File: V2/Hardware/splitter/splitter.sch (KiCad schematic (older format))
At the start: 17 parts, among them J0 Rpi_40Pin_F, J1 Control1_F, J2 Control2_F, J3 Control3_F, J4 Molex_PSU_F, J5 Siren, J6 USB_A_F, K0 RELRAS0515, Q0 BC548C, Q1 BD139-16

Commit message: update schemas
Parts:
- added D3: LED_2V_20mA, LED_THT:LED_D5.0mm, symbol Device:LED
- added R4: 510R, Resistor_THT:R_Axial_DIN0207_L6.3mm_D2.5mm_P10.16mm_Horizontal, symbol Device:R
- J1: value Control1_F -> Control_seg:1
- J2: value Control2_F -> Control_seg:2
- J3: value Control3_F -> Control_seg:3
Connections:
- net 12V+: now also R4.2
- net Earth: now also D3.1 (K)
- net seg:2_bit:a_gpio:10: now reaches J0.19 (Pin_19)
- net seg:2_bit:a_gpio:10: now also J2.4 (Pin_4)
- net seg:2_bit:b_gpio:09: now reaches J0.21 (Pin_21)
- net seg:2_bit:b_gpio:09: now also J2.3 (Pin_3)
- net seg:2_bit:c_gpio:11: now reaches J0.23 (Pin_23)
- net seg:2_bit:c_gpio:11: now also J2.2 (Pin_2)
- net seg:3_bit:d_gpio:26: now reaches J0.37 (Pin_37)
- net seg:3_bit:d_gpio:26: now also J3.1 (Pin_1)
- net 1a renamed seg:1_bit:d_gpio:22
- net 1b renamed seg:1_bit:c_gpio:27
- net 1c renamed seg:1_bit:b_gpio:17
- net 1d renamed seg:1_bit:a_gpio:04
- net 2a renamed seg:2_bit:d_gpio:05
- net seg:2_bit:d_gpio:05: now also J0.29 (Pin_29); no longer J0.35 (Pin_35)
- net 2b renamed seg:3_bit:b_gpio:13
- net seg:3_bit:b_gpio:13: now also J3.3 (Pin_3); no longer J2.2 (Pin_2)
- net 2c renamed seg:3_bit:a_gpio:06
- net seg:3_bit:a_gpio:06: now also J3.4 (Pin_4); no longer J2.3 (Pin_3)
- removed net 2d: J0.29 (Pin_29), J2.4 (Pin_4)
- net 3a renamed SIREN_gpio:21
- net SIREN_gpio:21: now also R1.2; no longer J3.1 (Pin_1)
- net 3b: no longer names the net of J0.38 (Pin_38)
- net 3b: no longer J3.2 (Pin_2)
- net 3c: no longer names the net of J0.36 (Pin_36)
- net 3c: no longer J3.3 (Pin_3)
- net 3d: no longer names the net of J0.32 (Pin_32)
- net 3d: no longer J3.4 (Pin_4)
- removed net BLANKING: J0.12 (Pin_12), J1.5 (Pin_5), J2.5 (Pin_5), J3.5 (Pin_5)
- net SIREN: no longer names the net of J0.16 (Pin_16)
- net SIREN: no longer R1.2
- new net: D3.2 (A), R4.1
- new net seg:3_bit:c_gpio:19: J0.35 (Pin_35), J3.2 (Pin_2)
- no-connect marks 32 -> 36
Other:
- moved on the sheet: D0, D1, D2, J0, J1, J2, J3, J4, J5, J6, K0, Q0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

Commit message: Finish PCBs
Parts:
- Q0: footprint Package_TO_SOT_THT:TO-92_Inline -> Package_TO_SOT_THT:TO-92_Inline_Wide
- R0: value 150R -> 33k
- R3, R4: value 510R -> 33k
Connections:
- net seg:1_bit:a_gpio:04: now also J1.6 (Pin_6); no longer J1.4 (Pin_4)
- net seg:1_bit:b_gpio:17: now also J1.5 (Pin_5); no longer J1.3 (Pin_3)
- net seg:1_bit:c_gpio:27: now also J1.3 (Pin_3); no longer J1.2 (Pin_2)
- net seg:2_bit:a_gpio:10: now also J2.6 (Pin_6); no longer J2.4 (Pin_4)
- net seg:2_bit:b_gpio:09: now also J2.5 (Pin_5); no longer J2.3 (Pin_3)
- net seg:2_bit:c_gpio:11: now also J2.3 (Pin_3); no longer J2.2 (Pin_2)
- net seg:3_bit:a_gpio:06: now also J3.6 (Pin_6); no longer J3.4 (Pin_4)
- net seg:3_bit:b_gpio:13: now also J3.5 (Pin_5); no longer J3.3 (Pin_3)
- net seg:3_bit:c_gpio:19: now also J3.3 (Pin_3); no longer J3.2 (Pin_2)
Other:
- moved on the sheet: J2, J3
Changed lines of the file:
@@
 L Connector_Generic:Conn_02x03_Counter_Clockwise J2
 U 1 1 5EA23348
-P 3950 4300
-F 0 "J2" H 4000 4617 50  0000 C CNN
-F 1 "Control_seg:2" H 4000 4526 50  0000 C CNN
-F 2 "Connector_PinHeader_2.54mm:PinHeader_2x03_P2.54mm_Horizontal" H 3950 4300 50  0001 C CNN
-F 3 "~" H 3950 4300 50  0001 C CNN
-	1    3950 4300
-	0    -1   -1   0
-$EndComp
-$Comp
-L Connector_Generic:Conn_02x03_Counter_Clockwise J3
-U 1 1 5EA246A5
-P 3450 5050
-F 0 "J3" H 3500 5367 50  0000 C CNN
-F 1 "Control_seg:3" H 3500 5276 50  0000 C CNN
-F 2 "Connector_PinHeader_2.54mm:PinHeader_2x03_P2.54mm_Horizontal" H 3450 5050 50  0001 C CNN
-F 3 "~" H 3450 5050 50  0001 C CNN
-	1    3450 5050
+P 3850 4300
+F 0 "J2" H 3900 4617 50  0000 C CNN
+F 1 "Control_seg:2" H 3900 4526 50  0000 C CNN
+F 2 "Connector_PinHeader_2.54mm:PinHeader_2x03_P2.54mm_Horizontal" H 3850 4300 50  0001 C CNN
+F 3 "~" H 3850 4300 50  0001 C CNN
+	1    3850 4300
 	0    -1   -1   0
 $EndComp
@@
 P 4450 2100
 F 0 "R0" H 4520 2146 50  0000 L CNN
-F 1 "150R" H 4520 2055 50  0000 L CNN
+F 1 "33k" H 4520 2055 50  0000 L CNN
 F 2 "Resistor_THT:R_Axial_DIN0207_L6.3mm_D2.5mm_P10.16mm_Horizontal" V 4380 2100 50  0001 C CNN
 F 3 "~" H 4450 2100 50  0001 C CNN
@@
 F 0 "Q0" H 7041 4446 50  0000 L CNN
 F 1 "BC548C" H 7041 4355 50  0000 L CNN
-F 2 "Package_TO_SOT_THT:TO-92_Inline" H 7050 4325 50  0001 L CIN
+F 2 "Package_TO_SOT_THT:TO-92_Inline_Wide" H 7050 4325 50  0001 L CIN
 F 3 "http://www.fairchildsemi.com/ds/BC/BC547.pdf" H 6850 4400 50  0001 L CNN
 	1    6850 4400
@@
 P 7250 3400
 F 0 "R3" H 7320 3446 50  0000 L CNN
-F 1 "510R" H 7320 3355 50  0000 L CNN
+F 1 "33k" H 7320 3355 50  0000 L CNN
 F 2 "Resistor_THT:R_Axial_DIN0207_L6.3mm_D2.5mm_P10.16mm_Horizontal" V 7180 3400 50  0001 C CNN
 F 3 "~" H 7250 3400 50  0001 C CNN
@@
 seg:3_bit:d_gpio:26
 Wire Wire Line
-	5600 4000 4700 4000
-Wire Wire Line
-	3850 5100 5600 5100
-Wire Wire Line
-	4700 4000 4700 3450
-Wire Wire Line
-	4700 3450 4550 3450
-Wire Wire Line
-	4350 4400 4350 3950
-Wire Wire Line
-	4350 4400 5600 4400
-Wire Wire Line
-	4450 4300 4450 3950
-Wire Wire Line
-	4450 4300 5600 4300
-Wire Wire Line
-	4550 4200 4550 3950
-Wire Wire Line
-	4550 4200 5600 4200
-Wire Wire Line
-	4200 4600 4200 4000
-Wire Wire Line
-	4200 4000 4050 4000
-Wire Wire Line
-	4200 4600 5600 4600
-Wire Wire Line
-	3850 5100 3850 4500
-Wire Wire Line
-	3950 4800 3950 4500
-Wire Wire Line
-	3950 4800 5600 4800
-Wire Wire Line
-	4050 4700 4050 4500
+	4750 4200 5600 4200
 Wire Wire Line
 	4050 4700 5600 4700
 Wire Wire Line
-	3700 5200 3700 4750
-Wire Wire Line
-	3700 4750 3550 4750
-Wire Wire Line
-	3700 5200 5600 5200
-Wire Wire Line
-	3550 5300 3550 5250
-Wire Wire Line
-	3550 5300 5600 5300
-Wire Wire Line
-	3450 5400 3450 5250
-Wire Wire Line
-	3450 5400 5600 5400
-Wire Wire Line
-	3350 5500 3350 5250
-Wire Wire Line
-	3350 5500 5600 5500
-NoConn ~ 4350 3450
-NoConn ~ 4450 3450
-NoConn ~ 3850 4000
-NoConn ~ 3950 4000
-NoConn ~ 3350 4750
-NoConn ~ 3450 4750
+	3450 5300 5600 5300
 $Comp
 L Device:R R4
@@
 P 5450 2550
 F 0 "R4" H 5520 2596 50  0000 L CNN
-F 1 "510R" H 5520 2505 50  0000 L CNN
+F 1 "33k" H 5520 2505 50  0000 L CNN
 F 2 "Resistor_THT:R_Axial_DIN0207_L6.3mm_D2.5mm_P10.16mm_Horizontal" V 5380 2550 50  0001 C CNN
 F 3 "~" H 5450 2550 50  0001 C CNN
@@
 Wire Wire Line
 	6300 2400 6600 2400
+Wire Wire Line
+	4850 4000 5600 4000
+Wire Wire Line
+	4750 4200 4750 3400
+Wire Wire Line
+	4750 3400 4450 3400
+Wire Wire Line
+	4450 3400 4450 3450
+Wire Wire Line
+	4550 4300 5600 4300
+Wire Wire Line
+	4150 4600 5600 4600
+Wire Wire Line
+	4050 4700 4050 3950
+Wire Wire Line
+	4050 3950 3850 3950
+Wire Wire Line
+	3850 3950 3850 4000
+Wire Wire Line
+	3950 4800 5600 4800
+Wire Wire Line
+	3550 5200 5600 5200
+Wire Wire Line
+	3450 5300 3450 4500
+Wire Wire Line
+	3450 4500 3250 4500
+Wire Wire Line
+	3350 5400 5600 5400
+NoConn ~ 3950 4000
+NoConn ~ 4550 3450
+Wire Wire Line
+	4550 4300 4550 3950
+Wire Wire Line
+	4350 4400 4350 3950
+Wire Wire Line
+	4350 4400 5600 4400
+Wire Wire Line
+	4850 4000 4850 3350
+Wire Wire Line
+	4850 3350 4350 3350
+Wire Wire Line
+	4350 3350 4350 3450
+NoConn ~ 4450 3950
+Wire Wire Line
+	3950 4800 3950 4500
+Wire Wire Line
+	4150 4600 4150 3900
+Wire Wire Line
+	4150 3900 3750 3900
+Wire Wire Line
+	3750 3900 3750 4000
+Wire Wire Line
+	3750 5100 5600 5100
+Wire Wire Line
+	3750 5100 3750 4500
+Wire Wire Line
+	3250 4500 3250 4550
+NoConn ~ 3350 4550
+$Comp
+L Connector_Generic:Conn_02x03_Counter_Clockwise J3
+U 1 1 5EA246A5
+P 3250 4850
+F 0 "J3" H 3300 5167 50  0000 C CNN
+F 1 "Control_seg:3" H 3300 5076 50  0000 C CNN
+F 2 "Connector_PinHeader_2.54mm:PinHeader_2x03_P2.54mm_Horizontal" H 3250 4850 50  0001 C CNN
+F 3 "~" H 3250 4850 50  0001 C CNN
+	1    3250 4850
+	0    -1   -1   0
+$EndComp
+Wire Wire Line
+	3350 5400 3350 5050
+Wire Wire Line
+	3150 5500 3150 5050
+Wire Wire Line
+	3150 5500 5600 5500
+Wire Wire Line
+	3550 5200 3550 4450
+Wire Wire Line
+	3550 4450 3150 4450
+Wire Wire Line
+	3150 4450 3150 4550
+NoConn ~ 3850 4500
+NoConn ~ 3250 5050
 $EndSCHEMATC

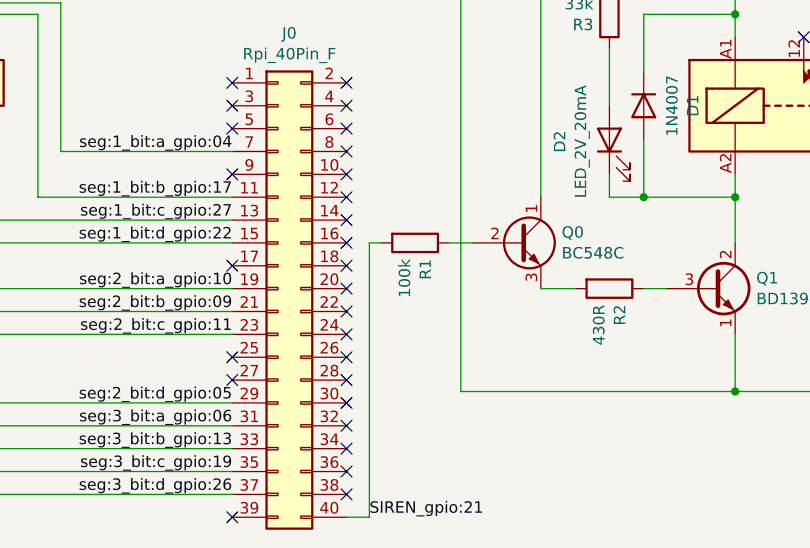
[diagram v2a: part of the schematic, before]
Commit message: Fix relay symbol
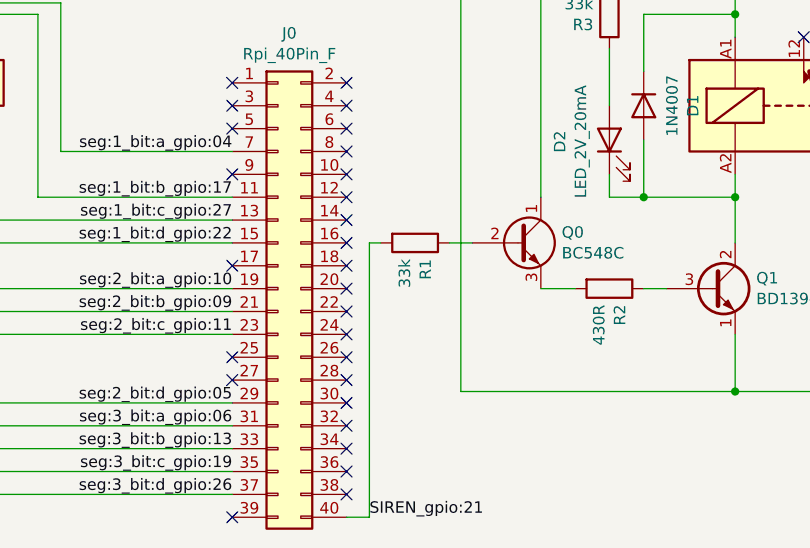
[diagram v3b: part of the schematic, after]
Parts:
- K0: footprint Relay_THT:Relay_SPDT_Finder_40.31 -> Relay_THT:Relay_SPDT_Finder_36.11
- R1: value 100k -> 33k
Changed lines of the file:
@@
 F 0 "K0" H 8430 3846 50  0000 L CNN
 F 1 "RELRAS0515" H 8430 3755 50  0000 L CNN
-F 2 "Relay_THT:Relay_SPDT_Finder_40.31" H 9140 3760 50  0001 C CNN
+F 2 "Relay_THT:Relay_SPDT_Finder_36.11" H 9140 3760 50  0001 C CNN
 F 3 "http://gfinder.findernet.com/assets/Series/353/S40EN.pdf" H 8000 3800 50  0001 C CNN
 	1    8000 3800
@@
 P 6400 4400
 F 0 "R1" H 6470 4446 50  0000 L CNN
-F 1 "100k" H 6470 4355 50  0000 L CNN
+F 1 "33k" H 6470 4355 50  0000 L CNN
 F 2 "Resistor_THT:R_Axial_DIN0207_L6.3mm_D2.5mm_P10.16mm_Horizontal" V 6330 4400 50  0001 C CNN
 F 3 "~" H 6400 4400 50  0001 C CNN

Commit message: Update splitter board
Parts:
- J0: footprint Connector_PinHeader_2.54mm:PinHeader_2x20_P2.54mm_Vertical -> Connector_IDC:IDC-Header_2x20_P2.54mm_Vertical
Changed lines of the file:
@@
 F 0 "J0" H 5850 5717 50  0000 C CNN
 F 1 "Rpi_40Pin_F" H 5850 5626 50  0000 C CNN
-F 2 "Connector_PinHeader_2.54mm:PinHeader_2x20_P2.54mm_Vertical" H 5800 4600 50  0001 C CNN
+F 2 "Connector_IDC:IDC-Header_2x20_P2.54mm_Vertical" H 5800 4600 50  0001 C CNN
 F 3 "~" H 5800 4600 50  0001 C CNN
 	1    5800 4600

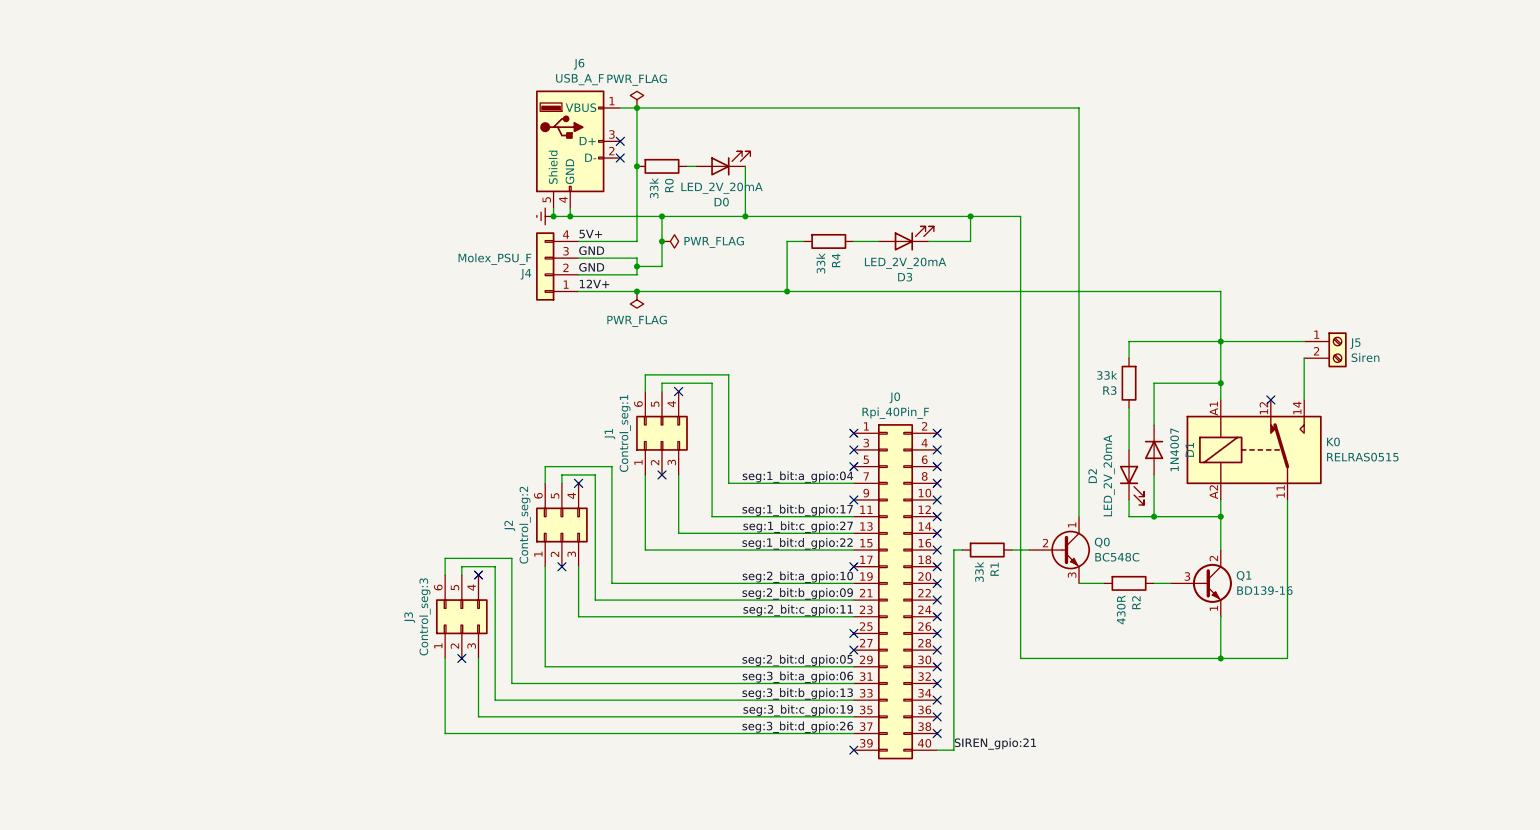
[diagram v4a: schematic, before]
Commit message: Simplify relay control
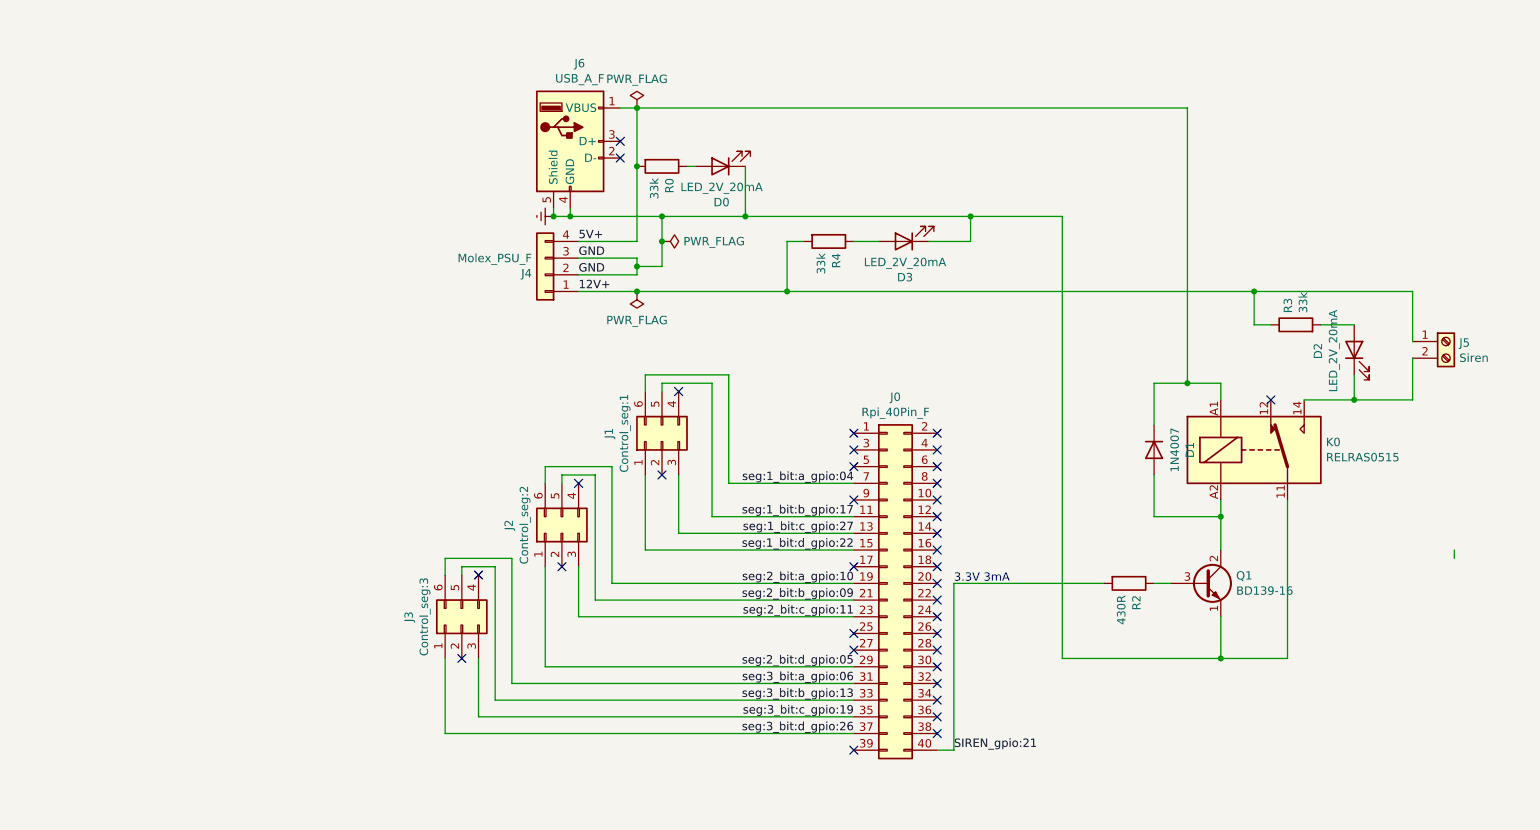
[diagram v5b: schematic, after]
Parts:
- removed Q0: BC548C, Package_TO_SOT_THT:TO-92_Inline_Wide, symbol Transistor_BJT:BC548
- removed R1: 33k, Resistor_THT:R_Axial_DIN0207_L6.3mm_D2.5mm_P10.16mm_Horizontal, symbol Device:R
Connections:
- net 12V+: now also R3.1; no longer D1.1 (K), K0.A1, R3.2
- net 5V+: now also D1.1 (K), K0.A1
- net SIREN_gpio:21: now also R2.2
- net at J5.2 (Pin_2), K0.14: now also D2.1 (K)
- net at D1.2 (A), K0.A2, Q1.2 (C): no longer D2.1 (K)
- net at D2.2 (A): now also R3.2; no longer R3.1
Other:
- note added: "3.3V 3mA"
- moved on the sheet: D2, J5, R3
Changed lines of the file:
@@
 L Connector:Screw_Terminal_01x02 J5
 U 1 1 5EBB14C8
-P 8500 3150
-F 0 "J5" H 8580 3142 50  0000 L CNN
-F 1 "Siren" H 8580 3051 50  0000 L CNN
-F 2 "TerminalBlock:TerminalBlock_bornier-2_P5.08mm" H 8500 3150 50  0001 C CNN
-F 3 "~" H 8500 3150 50  0001 C CNN
-	1    8500 3150
+P 9150 3150
+F 0 "J5" H 9230 3142 50  0000 L CNN
+F 1 "Siren" H 9230 3051 50  0000 L CNN
+F 2 "TerminalBlock:TerminalBlock_bornier-2_P5.08mm" H 9150 3150 50  0001 C CNN
+F 3 "~" H 9150 3150 50  0001 C CNN
+	1    9150 3150
 	1    0    0    -1
 $EndComp
@@
 $EndComp
 $Comp
-L Transistor_BJT:BC548 Q0
-U 1 1 5ED48271
-P 6850 4400
-F 0 "Q0" H 7041 4446 50  0000 L CNN
-F 1 "BC548C" H 7041 4355 50  0000 L CNN
-F 2 "Package_TO_SOT_THT:TO-92_Inline_Wide" H 7050 4325 50  0001 L CIN
-F 3 "http://www.fairchildsemi.com/ds/BC/BC547.pdf" H 6850 4400 50  0001 L CNN
-	1    6850 4400
-	1    0    0    -1
-$EndComp
-$Comp
 L Transistor_BJT:BD139 Q1
 U 1 1 5ED492AC
@@
 $EndComp
 Wire Wire Line
-	6550 4400 6650 4400
-$Comp
-L Device:R R1
-U 1 1 5ED47212
-P 6400 4400
-F 0 "R1" H 6470 4446 50  0000 L CNN
-F 1 "33k" H 6470 4355 50  0000 L CNN
-F 2 "Resistor_THT:R_Axial_DIN0207_L6.3mm_D2.5mm_P10.16mm_Horizontal" V 6330 4400 50  0001 C CNN
-F 3 "~" H 6400 4400 50  0001 C CNN
-	1    6400 4400
-	0    1    1    0
-$EndComp
-Wire Wire Line
-	6950 1750 6950 4200
-Wire Wire Line
-	4300 1750 6950 1750
-Wire Wire Line
-	7100 4600 6950 4600
-Wire Wire Line
 	7400 4600 7500 4600
 Wire Wire Line
 	4300 2850 5200 2850
 Wire Wire Line
-	6600 2400 6600 5050
-Wire Wire Line
-	6600 5050 7800 5050
+	6850 2400 6850 5050
+Wire Wire Line
+	6850 5050 7800 5050
 Wire Wire Line
 	7800 5050 7800 4800
@@
 Wire Wire Line
 	7800 4100 7800 4200
-Wire Wire Line
-	7800 2850 7800 3150
 Wire Wire Line
 	7800 4200 7400 4200
@@
 	7800 4200 7800 4400
 Wire Wire Line
-	7800 3400 7400 3400
+	7800 3400 7600 3400
 Wire Wire Line
 	7400 3400 7400 3650
-Connection ~ 7800 3400
 Wire Wire Line
 	7800 3400 7800 3500
-Wire Wire Line
-	8300 3150 7800 3150
-Connection ~ 7800 3150
-Wire Wire Line
-	7800 3150 7800 3400
-Wire Wire Line
-	8300 3500 8300 3250
 Wire Wire Line
 	8200 4100 8200 5050
@@
 L Device:LED D2
 U 1 1 5EDC36BC
-P 7250 3950
-F 0 "D2" H 7243 4166 50  0000 C CNN
-F 1 "LED_2V_20mA" H 7243 4075 50  0000 C CNN
-F 2 "LED_THT:LED_D5.0mm" H 7250 3950 50  0001 C CNN
-F 3 "~" H 7250 3950 50  0001 C CNN
-	1    7250 3950
+P 8600 3200
+F 0 "D2" H 8593 3416 50  0000 C CNN
+F 1 "LED_2V_20mA" H 8593 3325 50  0000 C CNN
+F 2 "LED_THT:LED_D5.0mm" H 8600 3200 50  0001 C CNN
+F 3 "~" H 8600 3200 50  0001 C CNN
+	1    8600 3200
 	0    -1   -1   0
 $EndComp
@@
 L Device:R R3
 U 1 1 5EDC8D2F
-P 7250 3400
-F 0 "R3" H 7320 3446 50  0000 L CNN
-F 1 "33k" H 7320 3355 50  0000 L CNN
-F 2 "Resistor_THT:R_Axial_DIN0207_L6.3mm_D2.5mm_P10.16mm_Horizontal" V 7180 3400 50  0001 C CNN
-F 3 "~" H 7250 3400 50  0001 C CNN
-	1    7250 3400
-	-1   0    0    1
-$EndComp
-Wire Wire Line
-	7250 3800 7250 3550
-Wire Wire Line
-	7250 3250 7250 3150
-Wire Wire Line
-	7250 3150 7800 3150
-Wire Wire Line
-	7250 4100 7250 4200
-Wire Wire Line
-	7250 4200 7400 4200
-Connection ~ 7400 4200
+P 8250 3050
+F 0 "R3" H 8320 3096 50  0000 L CNN
+F 1 "33k" H 8320 3005 50  0000 L CNN
+F 2 "Resistor_THT:R_Axial_DIN0207_L6.3mm_D2.5mm_P10.16mm_Horizontal" V 8180 3050 50  0001 C CNN
+F 3 "~" H 8250 3050 50  0001 C CNN
+	1    8250 3050
+	0    -1   -1   0
+$EndComp
+Wire Wire Line
+	9200 4450 9200 4400
 NoConn ~ 6100 4200
 $Comp
@@
 	6100 5600 6200 5600
 Wire Wire Line
-	6200 5600 6200 4400
-Wire Wire Line
-	6200 4400 6250 4400
+	6200 5600 6200 4600
 Text Label 6200 5600 0    50   ~ 0
 SIREN_gpio:21
@@
 Connection ~ 5200 2850
 Wire Wire Line
-	5200 2850 7800 2850
-Wire Wire Line
 	5600 2550 5750 2550
 Wire Wire Line
@@
 Connection ~ 6300 2400
 Wire Wire Line
-	6300 2400 6600 2400
+	6300 2400 6850 2400
 Wire Wire Line
 	4850 4000 5600 4000
@@
 NoConn ~ 3850 4500
 NoConn ~ 3250 5050
+Wire Wire Line
+	6200 4600 7100 4600
+Wire Wire Line
+	7600 3400 7600 1750
+Wire Wire Line
+	4300 1750 7600 1750
+Connection ~ 7600 3400
+Wire Wire Line
+	7600 3400 7400 3400
+Wire Wire Line
+	8950 2850 8950 3150
+Wire Wire Line
+	5200 2850 8000 2850
+Wire Wire Line
+	8300 3500 8600 3500
+Wire Wire Line
+	8950 3500 8950 3250
+Wire Wire Line
+	8600 3050 8400 3050
+Wire Wire Line
+	8100 3050 8000 3050
+Wire Wire Line
+	8000 3050 8000 2850
+Connection ~ 8000 2850
+Wire Wire Line
+	8000 2850 8950 2850
+Wire Wire Line
+	8600 3350 8600 3500
+Connection ~ 8600 3500
+Wire Wire Line
+	8600 3500 8950 3500
+Text Notes 6200 4600 0    50   ~ 0
+3.3V 3mA
 $EndSCHEMATC
